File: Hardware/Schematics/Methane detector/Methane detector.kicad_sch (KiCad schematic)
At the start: 4 parts, among them U1 ESP32-DEVKIT-V1

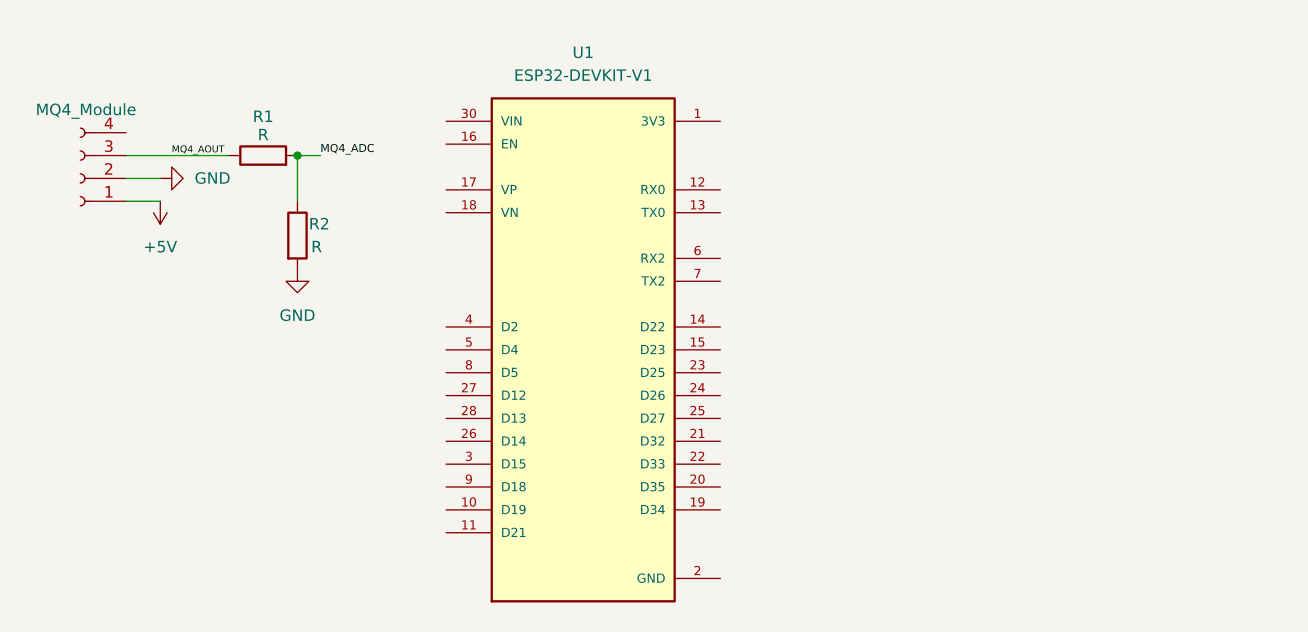
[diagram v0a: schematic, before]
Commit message: feat: Added alarm system with leds and buzzer
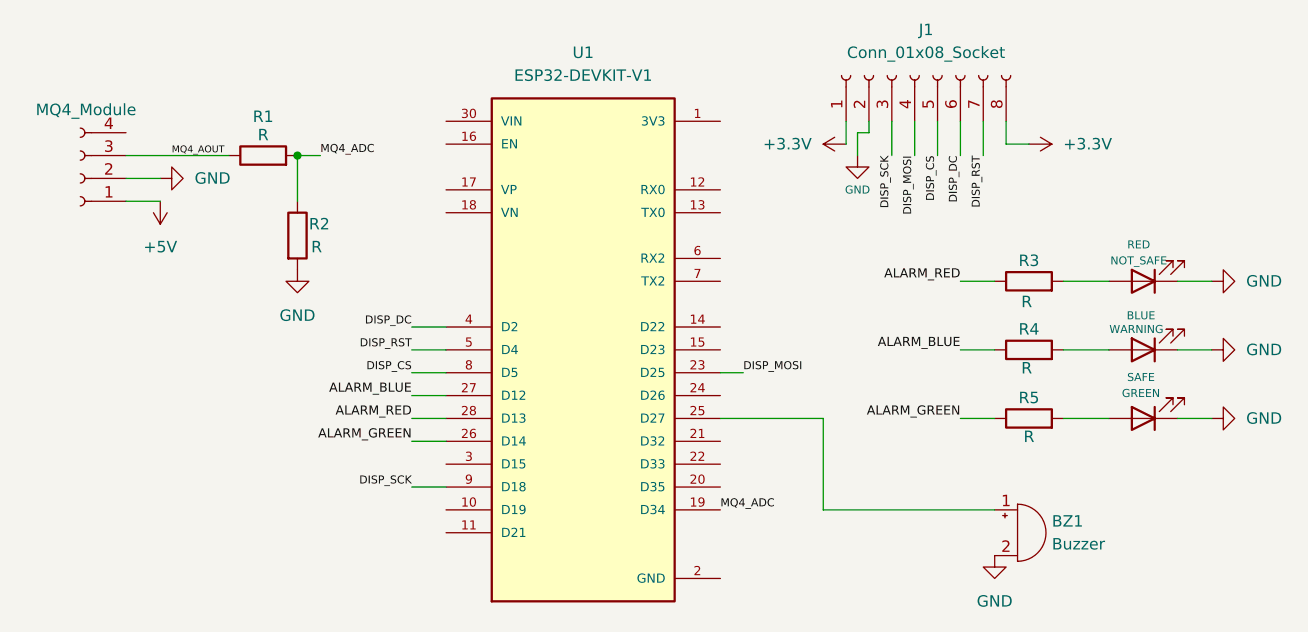
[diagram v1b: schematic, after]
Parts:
- added BLUE: WARNING, symbol Device:LED
- added BZ1: Buzzer, symbol Device:Buzzer
- added J1: Conn_01x08_Socket, symbol Connector:Conn_01x08_Socket
- added R3, R4, R5: R, symbol Device:R
- added RED: NOT_SAFE, symbol Device:LED
- added SAFE: GREEN, symbol Device:LED
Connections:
- net GND: now also BLUE.1 (K), BZ1.2 (-), J1.2 (Pin_2), RED.1 (K), SAFE.1 (K)
- net MQ4_ADC: now also U1.19 (D34)
- net DISP_MOSI: now reaches U1.23 (D25)
- net DISP_MOSI: now also J1.4 (Pin_4)
- net at U1.25 (D27): now also BZ1.1 (+)
- net ALARM_GREEN: now reaches U1.26 (D14)
- net ALARM_GREEN: now also R5.1
- net ALARM_BLUE: now reaches U1.27 (D12)
- net ALARM_BLUE: now also R4.1
- net ALARM_RED: now reaches U1.28 (D13)
- net ALARM_RED: now also R3.1
- net DISP_DC: now reaches U1.4 (D2)
- net DISP_DC: now also J1.6 (Pin_6)
- net DISP_RST: now reaches U1.5 (D4)
- net DISP_RST: now also J1.7 (Pin_7)
- net DISP_CS: now reaches U1.8 (D5)
- net DISP_CS: now also J1.5 (Pin_5)
- net DISP_SCK: now reaches U1.9 (D18)
- net DISP_SCK: now also J1.3 (Pin_3)
- new net: R5.2, SAFE.2 (A)
- new net: R3.2, RED.2 (A)
- new net: BLUE.2 (A), R4.2
- new net +3.3V: J1.1 (Pin_1), J1.8 (Pin_8)

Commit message: style: remove unnecessary PCB and junk files for clean repo
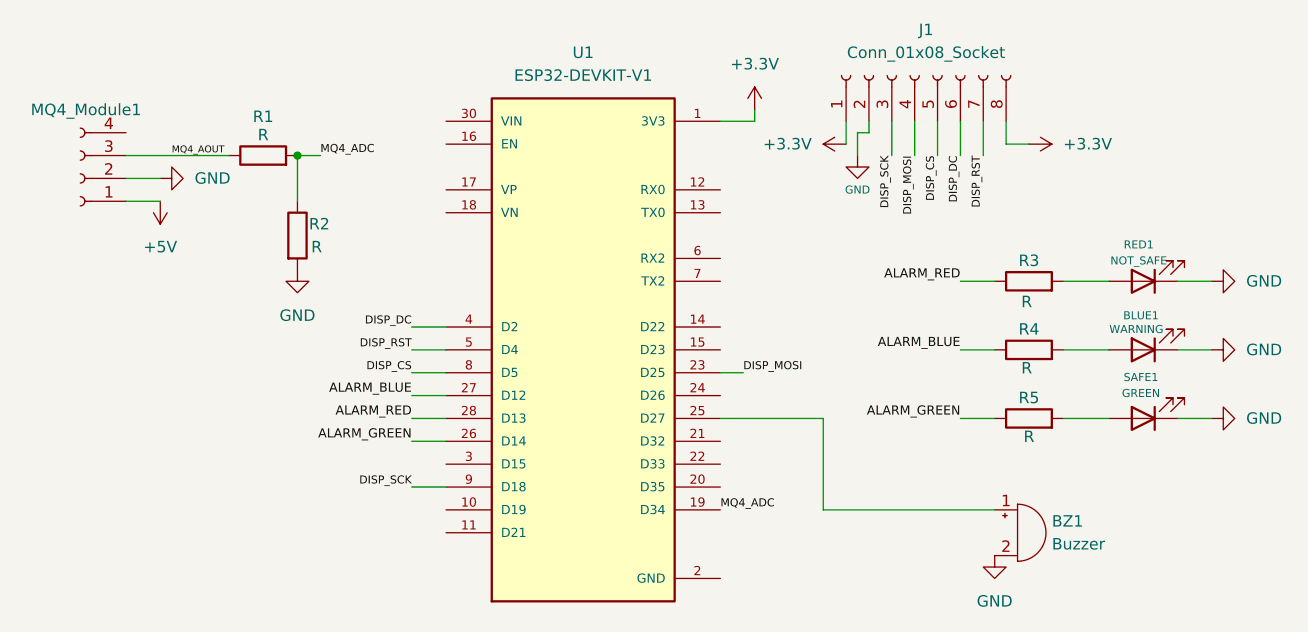
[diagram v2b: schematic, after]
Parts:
- renumbered BLUE to BLUE1, MQ4_Module to MQ4_Module1, RED to RED1, SAFE to SAFE1
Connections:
- net +3.3V: now also U1.1 (3V3)
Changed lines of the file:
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@@
+	(wire
+		(pts
+			(xy 104.14 33.02) (xy 107.95 33.02)
+		)
+		(stroke
+			(width 0)
+			(type default)
+		)
+	)
 	(wire
 		(pts
@@
 		(pts
 			(xy 119.38 34.29) (xy 119.38 36.83)
+		)
+		(stroke
+			(width 0)
+			(type default)
+		)
+	)
+	(wire
+		(pts
+			(xy 107.95 33.02) (xy 107.95 31.75)
 		)
 		(stroke
@@
 		(dnp no)
 		(fields_autoplaced yes)
-		(property "Reference" "MQ4_Module"
+		(property "Reference" "MQ4_Module1"
 			(at 33.655 31.75 0)
 			(effects
@@
 			(project ""
 				(path "/3eac1686-6fd7-4e6d-8fbf-da3df28626a1"
-					(reference "MQ4_Module")
+					(reference "MQ4_Module1")
 					(unit 1)
 				)
@@
 		(on_board yes)
 		(dnp no)
-		(property "Reference" "BLUE"
+		(property "Reference" "BLUE1"
 			(at 150.876 54.61 0)
 			(effects
@@
 			(project "Methane detector"
 				(path "/3eac1686-6fd7-4e6d-8fbf-da3df28626a1"
-					(reference "BLUE")
+					(reference "BLUE1")
 					(unit 1)
 				)
@@
 		(on_board yes)
 		(dnp no)
-		(property "Reference" "RED"
+		(property "Reference" "RED1"
 			(at 150.622 46.736 0)
 			(effects
@@
 			(project ""
 				(path "/3eac1686-6fd7-4e6d-8fbf-da3df28626a1"
-					(reference "RED")
+					(reference "RED1")
 					(unit 1)
 				)
@@
 	)
 	(symbol
+		(lib_id "power:+3.3V")
+		(at 107.95 31.75 0)
+		(unit 1)
+		(exclude_from_sim no)
+		(in_bom yes)
+		(on_board yes)
+		(dnp no)
+		(fields_autoplaced yes)
+		(property "Reference" "#PWR011"
+			(at 107.95 35.56 0)
+			(effects
+				(font
+					(size 1.27 1.27)
+				)
+				(hide yes)
+			)
+		)
+		(property "Value" "+3.3V"
+			(at 107.95 26.67 0)
+			(effects
+				(font
+					(size 1.27 1.27)
+				)
+			)
+		)
+		(property "Footprint" ""
+			(at 107.95 31.75 0)
+			(effects
+				(font
+					(size 1.27 1.27)
+				)
+				(hide yes)
+			)
+		)
+		(property "Datasheet" ""
+			(at 107.95 31.75 0)
+			(effects
+				(font
+					(size 1.27 1.27)
+				)
+				(hide yes)
+			)
+		)
+		(property "Description" "Power symbol creates a global label with name \"+3.3V\""
+			(at 107.95 31.75 0)
+			(effects
+				(font
+					(size 1.27 1.27)
+				)
+				(hide yes)
+			)
+		)
+		(pin "1"
+		)
+		(instances
+			(project ""
+				(path "/3eac1686-6fd7-4e6d-8fbf-da3df28626a1"
+					(reference "#PWR011")
+					(unit 1)
+				)
+			)
+		)
+	)
+	(symbol
 		(lib_id "Device:LED")
 		(at 151.13 66.04 180)
@@
 		(on_board yes)
 		(dnp no)
-		(property "Reference" "SAFE"
+		(property "Reference" "SAFE1"
 			(at 150.876 61.468 0)
 			(effects
@@
 			(project "Methane detector"
 				(path "/3eac1686-6fd7-4e6d-8fbf-da3df28626a1"
-					(reference "SAFE")
+					(reference "SAFE1")
 					(unit 1)
 				)
